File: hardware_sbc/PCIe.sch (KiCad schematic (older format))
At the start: 23 parts, among them J5 Bus_PCI_Express_Mini, U1 IMX8MM, U13 MIC94164

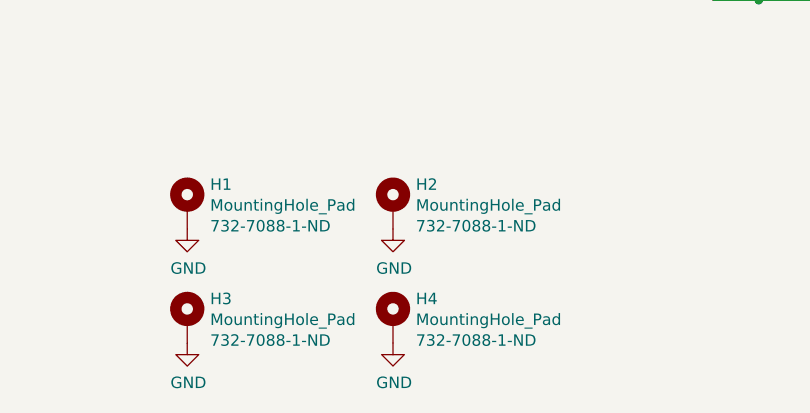
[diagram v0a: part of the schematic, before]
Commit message: Remove standoffs from board and update 3d model
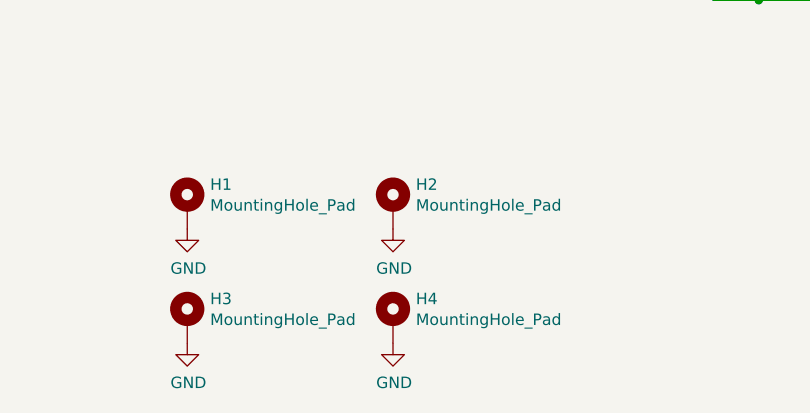
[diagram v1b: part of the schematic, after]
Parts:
- H1, H2, H3, H4: footprint mxenc:MountingHole_M2_Standoff -> mxenc:MountingHole_M2_Hole; Mfgr Wurth -> (none); Mfgrpart 9774035243R‎ -> (none); Vendorpart 732-7088-1-ND‎ -> (none)
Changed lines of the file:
@@
 Connection ~ 5250 5500
-$Comp
-L Mechanical:MountingHole_Pad H1
-U 1 1 5EF33699
-P 2750 6400
-F 0 "H1" H 2850 6494 50  0000 L CNN
-F 1 "MountingHole_Pad" H 2850 6403 50  0000 L CNN
-F 2 "mxenc:MountingHole_M2_Standoff" H 2750 6400 50  0001 C CNN
-F 3 "~" H 2750 6400 50  0001 C CNN
-F 4 "732-7088-1-ND‎" H 2850 6312 50  0000 L CNN "Vendorpart"
-F 5 "Wurth" H 2750 6400 50  0001 C CNN "Mfgr"
-F 6 "" H 2750 6400 50  0001 C CNN "Part"
-F 7 "9774035243R‎" H 2750 6400 50  0001 C CNN "Mfgrpart"
-	1    2750 6400
-	1    0    0    -1
-$EndComp
 $Comp
 L power:GND #PWR0224
@@
 F 0 "H2" H 3750 6494 50  0000 L CNN
 F 1 "MountingHole_Pad" H 3750 6403 50  0000 L CNN
-F 2 "mxenc:MountingHole_M2_Standoff" H 3650 6400 50  0001 C CNN
-F 3 "~" H 3650 6400 50  0001 C CNN
-F 4 "732-7088-1-ND‎" H 3750 6312 50  0000 L CNN "Vendorpart"
-F 5 "Wurth" H 3650 6400 50  0001 C CNN "Mfgr"
-F 6 "" H 3650 6400 50  0001 C CNN "Part"
-F 7 "9774035243R‎" H 3650 6400 50  0001 C CNN "Mfgrpart"
+F 2 "mxenc:MountingHole_M2_Hole" H 3650 6400 50  0001 C CNN
+F 3 "" H 3650 6400 50  0001 C CNN
+F 4 "" H 3650 6400 50  0001 C CNN "Part"
 	1    3650 6400
 	1    0    0    -1
@@
 F 0 "H4" H 3750 6994 50  0000 L CNN
 F 1 "MountingHole_Pad" H 3750 6903 50  0000 L CNN
-F 2 "mxenc:MountingHole_M2_Standoff" H 3650 6900 50  0001 C CNN
-F 3 "~" H 3650 6900 50  0001 C CNN
-F 4 "732-7088-1-ND‎" H 3750 6812 50  0000 L CNN "Vendorpart"
-F 5 "Wurth" H 3650 6900 50  0001 C CNN "Mfgr"
-F 6 "" H 3650 6900 50  0001 C CNN "Part"
-F 7 "9774035243R‎" H 3650 6900 50  0001 C CNN "Mfgrpart"
+F 2 "mxenc:MountingHole_M2_Hole" H 3650 6900 50  0001 C CNN
+F 3 "" H 3650 6900 50  0001 C CNN
+F 4 "" H 3650 6900 50  0001 C CNN "Part"
 	1    3650 6900
 	1    0    0    -1
@@
 F 0 "H3" H 2850 6994 50  0000 L CNN
 F 1 "MountingHole_Pad" H 2850 6903 50  0000 L CNN
-F 2 "mxenc:MountingHole_M2_Standoff" H 2750 6900 50  0001 C CNN
-F 3 "~" H 2750 6900 50  0001 C CNN
-F 4 "732-7088-1-ND‎" H 2850 6812 50  0000 L CNN "Vendorpart"
-F 5 "Wurth" H 2750 6900 50  0001 C CNN "Mfgr"
-F 6 "" H 2750 6900 50  0001 C CNN "Part"
-F 7 "9774035243R‎" H 2750 6900 50  0001 C CNN "Mfgrpart"
+F 2 "mxenc:MountingHole_M2_Hole" H 2750 6900 50  0001 C CNN
+F 3 "" H 2750 6900 50  0001 C CNN
+F 4 "" H 2750 6900 50  0001 C CNN "Part"
 	1    2750 6900
 	1    0    0    -1
@@
 	1    0    0    -1
 $EndComp
+$Comp
+L Mechanical:MountingHole_Pad H1
+U 1 1 5EF33699
+P 2750 6400
+F 0 "H1" H 2850 6494 50  0000 L CNN
+F 1 "MountingHole_Pad" H 2850 6403 50  0000 L CNN
+F 2 "mxenc:MountingHole_M2_Hole" H 2750 6400 50  0001 C CNN
+F 3 "" H 2750 6400 50  0001 C CNN
+F 4 "" H 2750 6400 50  0001 C CNN "Part"
+	1    2750 6400
+	1    0    0    -1
+$EndComp
